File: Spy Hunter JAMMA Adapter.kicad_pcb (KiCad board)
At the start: 2 copper layers, 111.4 x 135.4 mm, 92 parts, among them P1 1K, P2 1K, P3 10K, P4 1K, SW2 SW_DIP_SPSTx02_Slide_9.78x7.2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, U1 74LS86, U10 NE555, U11 LM386, U12 CD4099B, U2 74LS74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

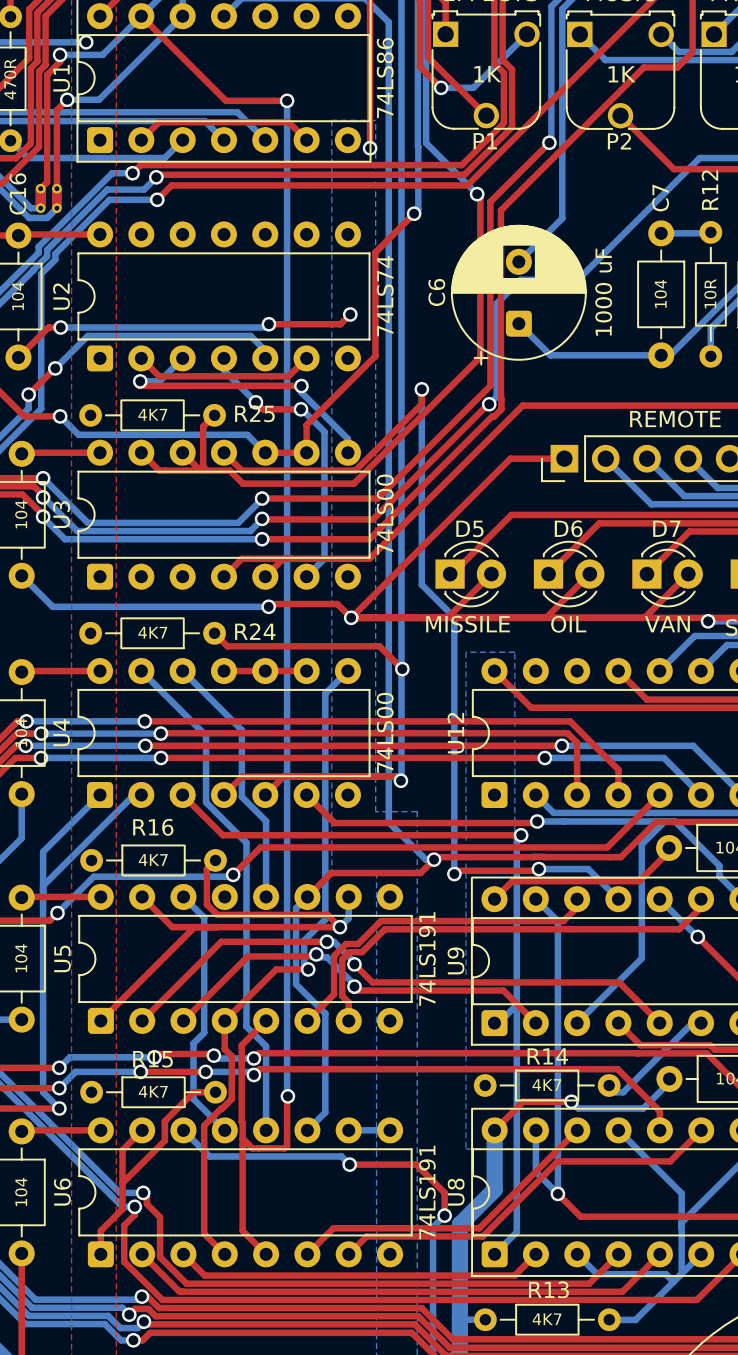
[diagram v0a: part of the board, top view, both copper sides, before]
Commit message: 0x8c is expressed as 2s complement, not 1s complement
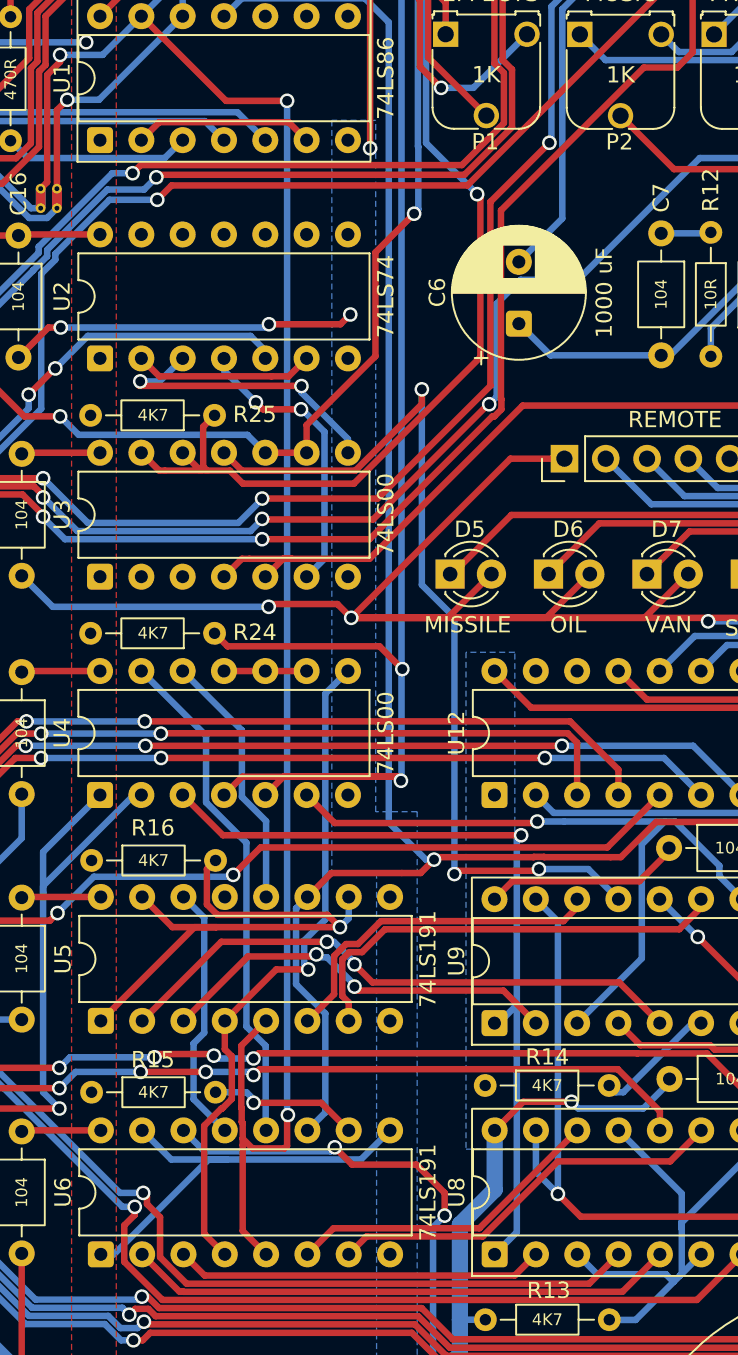
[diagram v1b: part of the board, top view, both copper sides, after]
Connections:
- U6 pad 1: +5V_R15 -> GND
- U6 pad 10: GND -> +5V_R15
- U6 pad 15: +5V_R15 -> GND
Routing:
- net GND: track 1284.6 -> 1308.9 mm
- net +5V_R15: track 17.4 -> 9.00 mm, vias 0 -> 1

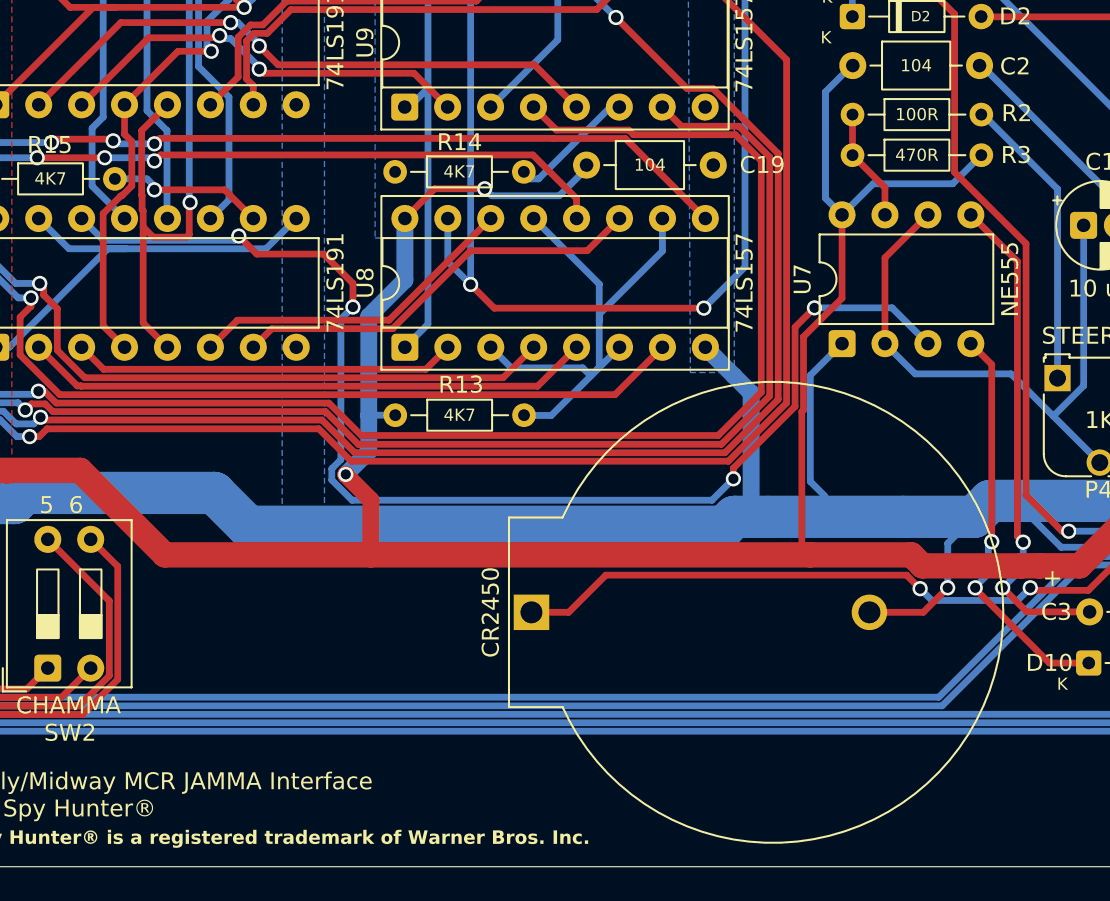
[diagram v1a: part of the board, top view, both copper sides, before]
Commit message: add pull-down resistor for U7
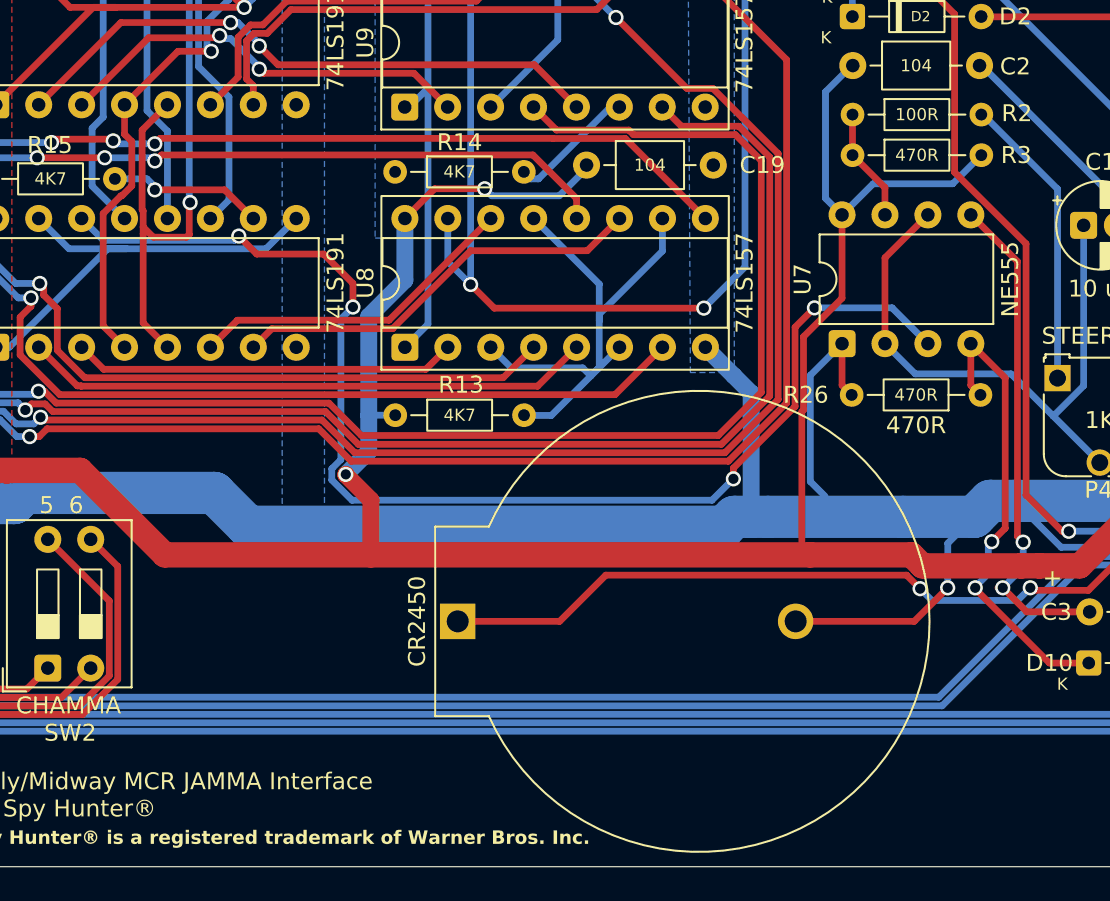
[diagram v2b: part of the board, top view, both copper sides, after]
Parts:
- added R26: 470R, R_Axial_DIN0204_L3.6mm_D1.6mm_P7.62mm_Horizontal, F.Cu at (136.1, 134.0)
- moved CR2450 4.40 mm to (105.2, 147.4)
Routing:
- net GND: track 1308.9 -> 1316.8 mm
- net BATT+: track 79.7 -> 84.2 mm
- net U7_RESET: track 24.0 -> 27.9 mm

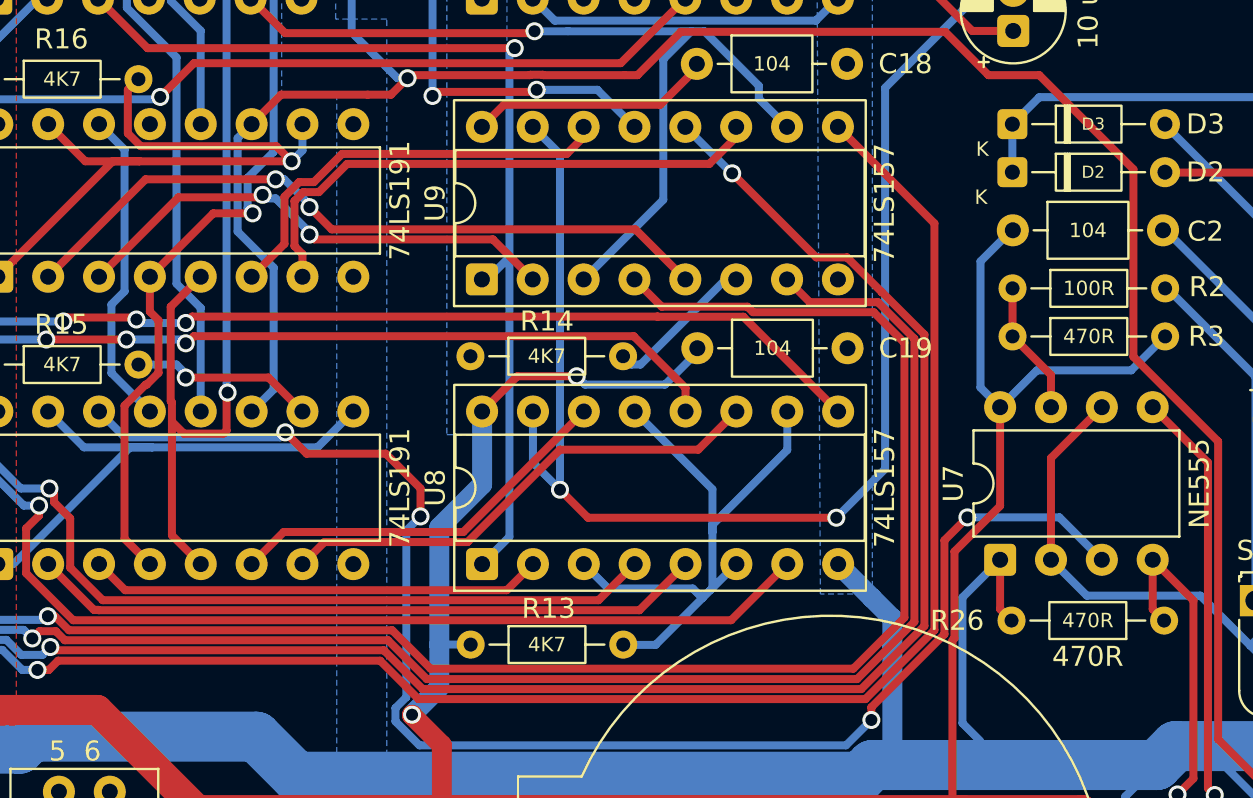
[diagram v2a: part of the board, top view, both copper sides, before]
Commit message: cause high counter to disable low counter on max/min to give us 4 bits of cushion
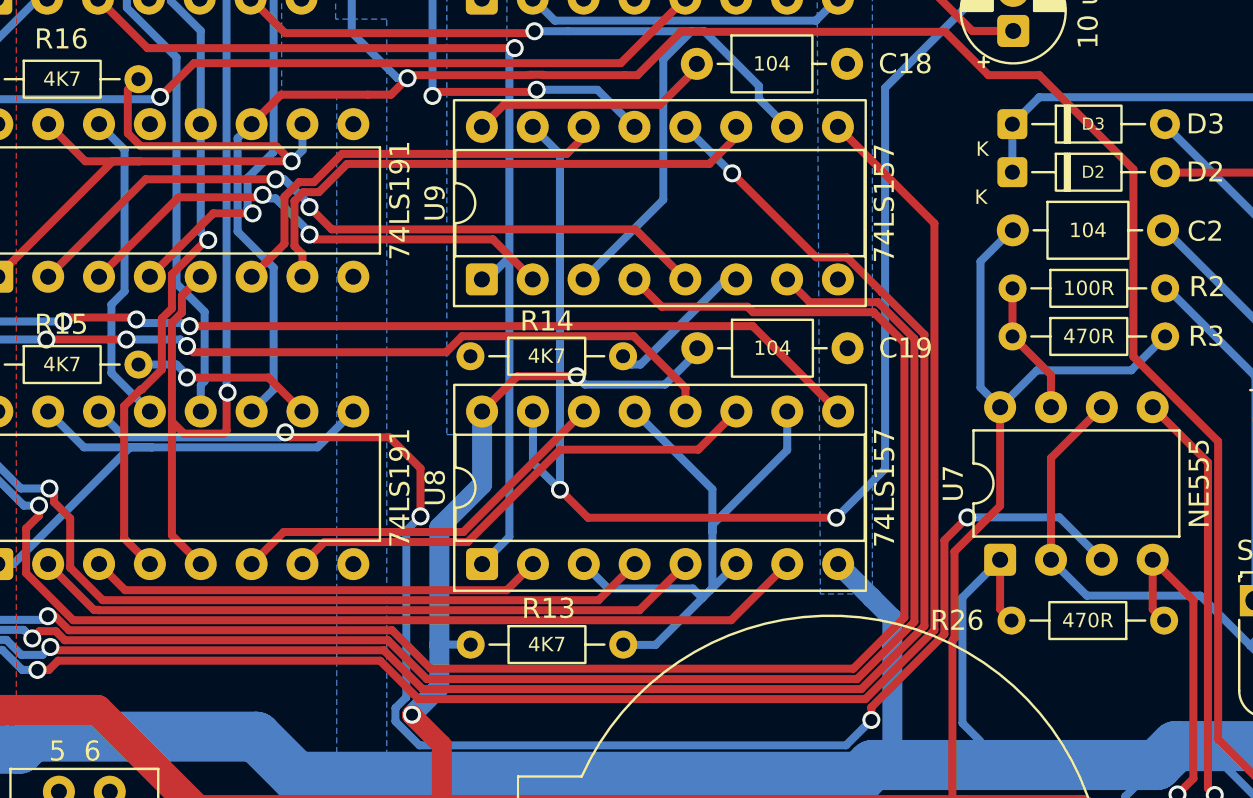
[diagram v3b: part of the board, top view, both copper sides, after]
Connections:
- U6 pad 4: CTEN -> U5_MAXMIN
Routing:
- net U5_MAXMIN: track 16.0 -> 40.5 mm, vias 0 -> 1
- net CTEN: track 41.8 -> 26.0 mm
- net CLK: track 74.5 -> 75.1 mm

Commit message: reduce logic
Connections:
- U4 pad 10: MAXMIN -> (no net)
- U4 pad 11: MAXMIN -> (no net)
- U4 pad 12: U5_MAXMIN -> (no net)
- U4 pad 13: U6_MAXMIN -> (no net)
- U4 pad 8: CTEN -> (no net)
- U4 pad 9: MAXMIN -> (no net)
- U5 pad 12: U5_MAXMIN -> MAXMIN_CTEN
- U5 pad 4: CTEN -> MAXMIN_CTEN
- U6 pad 12: U6_MAXMIN -> (no net)
- U6 pad 4: U5_MAXMIN -> MAXMIN_CTEN
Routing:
- net U5_MAXMIN: track 40.5 -> 0.00 mm, vias 1 -> 0
- net U6_MAXMIN: track 31.6 -> 0.00 mm
- net CTEN: track 26.0 -> 0.00 mm, vias 1 -> 0
- net MAXMIN_CTEN: track 0.00 -> 24.3 mm
- net MAXMIN: track 5.08 -> 0.00 mm
- net U6_RCO: track 15.9 -> 16.6 mm

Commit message: 3.96 for power, rework board a bit
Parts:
- removed CSQDJ2, MCRJ1A: Molex_KK-254_AE-6410-05A_1x05_P2.54mm_Vertical, Connector_Molex:Molex_KK-254_AE-6410-05A_1x05_P2.54mm_Vertical
- removed MCRJ1B: Molex_KK-254_AE-6410-07A_1x07_P2.54mm_Vertical, Connector_Molex:Molex_KK-254_AE-6410-07A_1x07_P2.54mm_Vertical
- added MCRJ1: Molex_KK-396_5273-12A_1x12_P3.96mm_Vertical, Connector_Molex:Molex_KK-396_5273-12A_1x12_P3.96mm_Vertical, F.Cu at (159.4, 92.4)
- added MCRJ1: Molex_KK-396_5273-05A_1x05_P3.96mm_Vertical, Connector_Molex:Molex_KK-396_5273-05A_1x05_P3.96mm_Vertical, F.Cu at (159.2, 115.8)
- EXT: renamed from JAMMA EXT
- moved C3 3.63 mm to (139.3, 148.3)
- moved D10 3.60 mm to (139.2, 151.2)
- moved CSQD - J1 2.81 mm to (159.4, 139.8)
- moved CSQDJ3 2.66 mm to (159.4, 122.4)
- moved D1 1.23 mm to (140.6, 103.4)
- moved CR2450 0.80 mm to (104.4, 147.4)
- moved PMH3 0.79 mm to (71.6, 157.4)
- moved PMH2 0.73 mm to (148.6, 157.4)
- moved PMH1 0.64 mm to (71.8, 46.2)
- moved PMH4 0.56 mm to (148.8, 46.3)
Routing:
- net +5V: track 570.3 -> 529.4 mm
- net GND: track 1316.8 -> 1352.2 mm
- net V.BATT: track 44.8 -> 73.9 mm, vias 1 -> 3
- net +5V_RST: track 54.5 -> 74.1 mm
- net J5_ST0: track 99.5 -> 102.9 mm
- net MUSIC_R: track 113.1 -> 115.8 mm
- net U12_A0: track 188.9 -> 191.1 mm
- net MUSIC_RV12: track 107.4 -> 109.6 mm
- net MUSIC_RVR: track 113.0 -> 115.2 mm
- net MUSIC_L: track 121.6 -> 123.6 mm
- net U7_CTL: track 29.9 -> 28.0 mm
- net U12_DATA: track 192.9 -> 194.7 mm
- net MUSIC_RVS: track 106.2 -> 107.8 mm
- net U12_A1: track 194.0 -> 195.5 mm
- net CLK_GATE: track 180.0 -> 178.6 mm
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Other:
- board text added: "CHEAP SQUEAK DELUXE"
- board text added: "J1 - DATA"
- board text added: "J3 - MUSIC"
- board text added: "Rev. 1"
- board text added: "Spy Hunter® is a registered trademark of Warner Bros. Entertainment Inc."
- board text removed: "CSD J1 - DATA"
- board text removed: "CSD J2 - POWER"
- board text removed: "CSD J3 - MUSIC"
- board text removed: "Spy Hunter® is a registered trademark of Warner Bros. Inc."
